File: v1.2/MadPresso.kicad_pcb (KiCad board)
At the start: 2 copper layers, 108 x 57.5 mm, 75 parts, among them J1 Conn_01x07, J2 Conn_01x03, J3 Conn_01x02, J4 Conn_01x04, Q1 BC847, Q2 BSS84, Q3 T835-600B, Q4 2N7002, Q5 T835-600B, Q6 2N7002, Q7 T835-600B, Q8 2N7002, U1 LTV-356T, U2 ADC101C021CIMK, U3 WeMos_D1_mini, U4 MID400, U5 MID400, U6 TLP160G, U7 TLP160G, U8 TLP160G

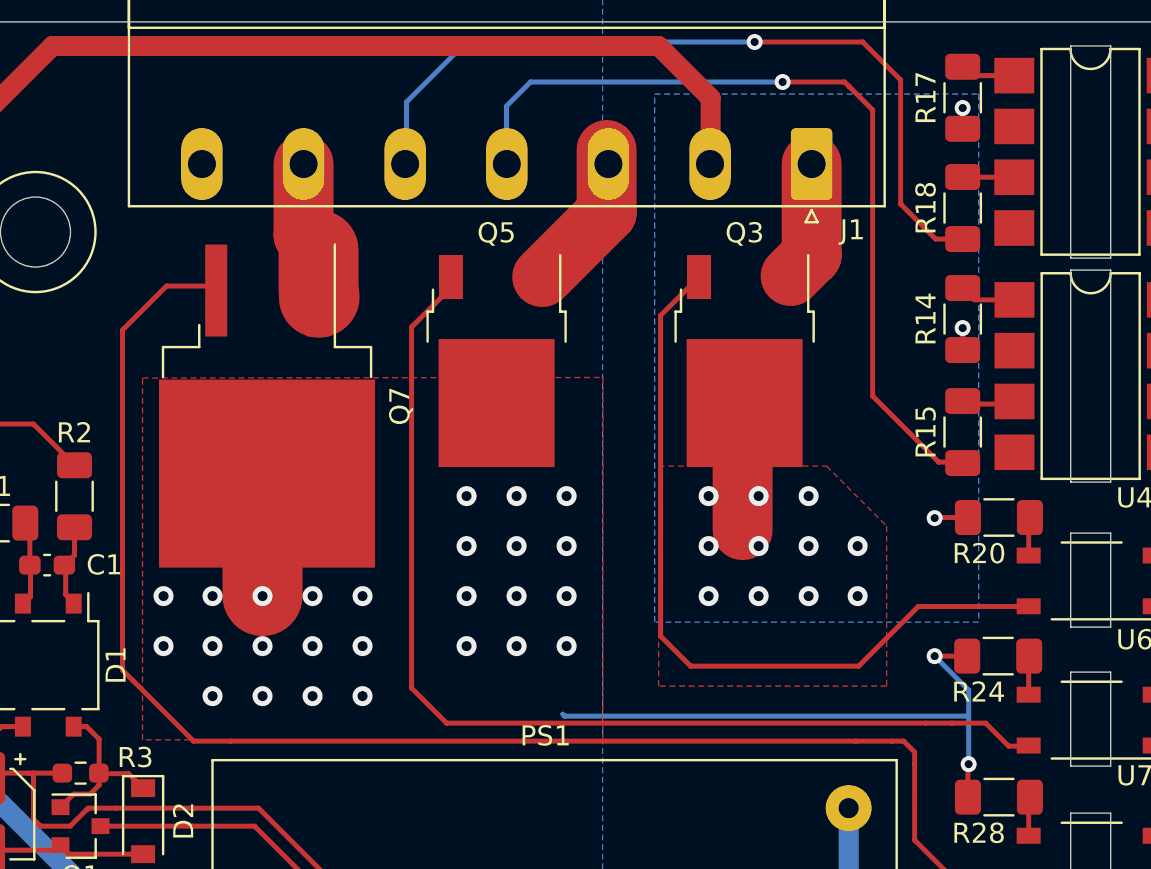
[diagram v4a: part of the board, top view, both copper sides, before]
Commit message: Revert Q7 back to DPAK
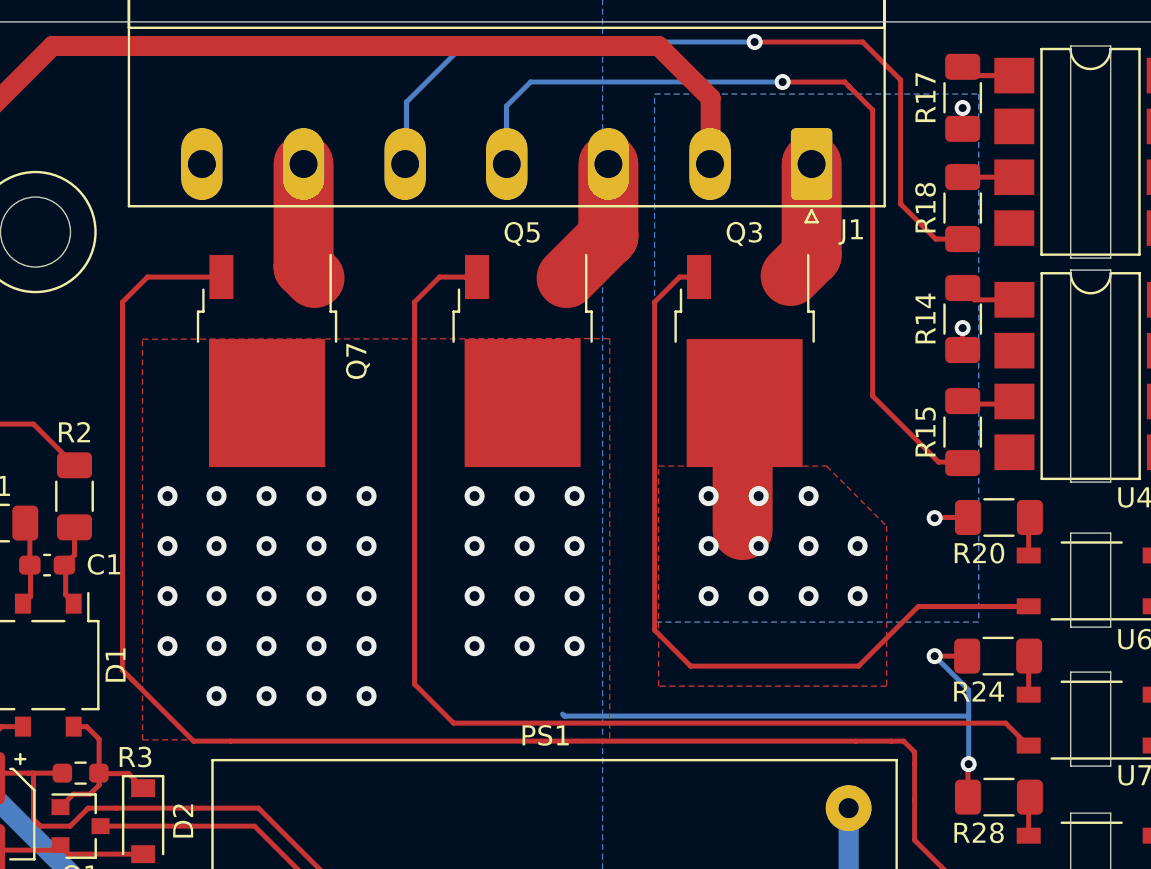
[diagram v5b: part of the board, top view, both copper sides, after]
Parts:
- Q7: footprint Package_TO_SOT_SMD:TO-263-2 -> Package_TO_SOT_SMD:TO-252-2
- moved Q7 2.25 mm to (26.8, 16.9)
- moved Q5 1.30 mm to (39.6, 16.9)
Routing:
- net LINE: track 35.7 -> 29.8 mm, vias 28 -> 38
- net Net-(Q7-Pad3): track 74.9 -> 76.2 mm
- net /VALVE: track 7.68 -> 6.57 mm
- net Net-(Q5-Pad3): track 53.4 -> 54.4 mm
- net Net-(Q3-Pad3): track 39.0 -> 39.8 mm
- net /HEATER: track 6.65 -> 5.93 mm

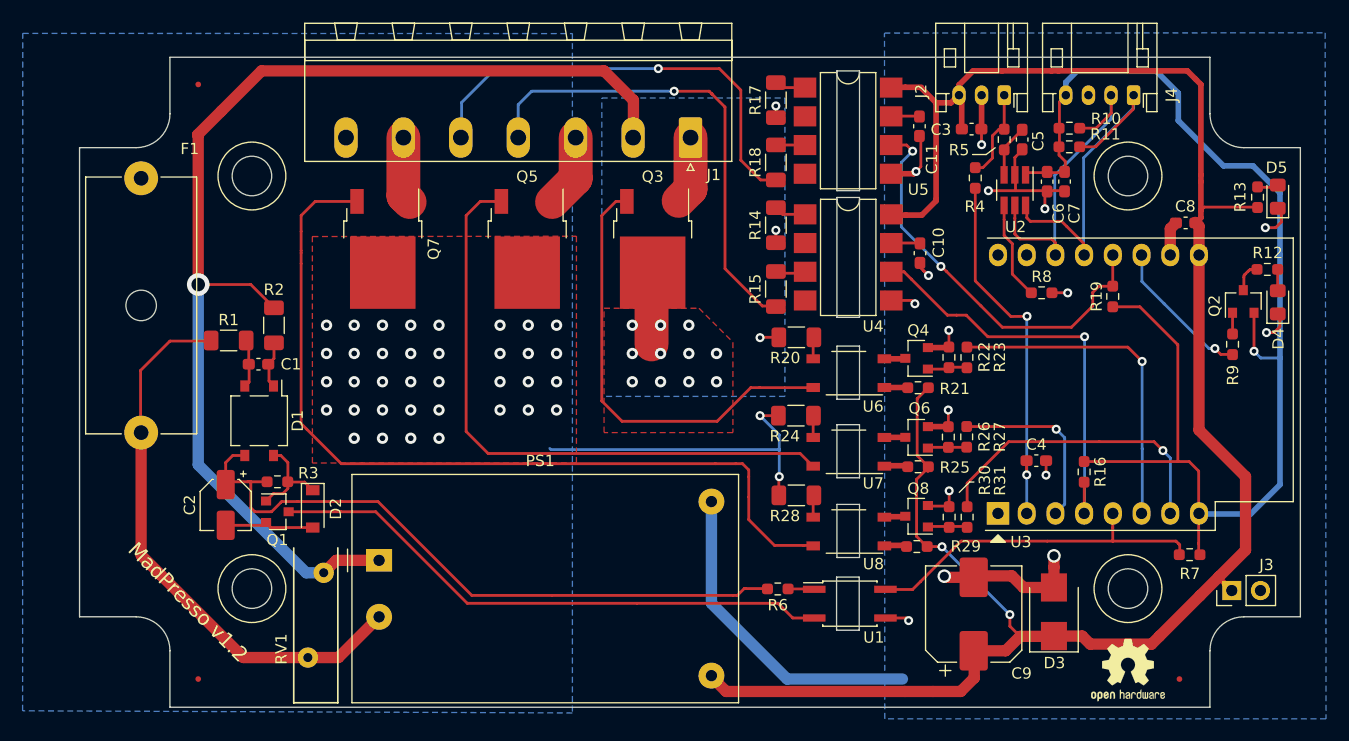
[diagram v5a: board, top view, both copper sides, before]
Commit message: trace widths and clearance details
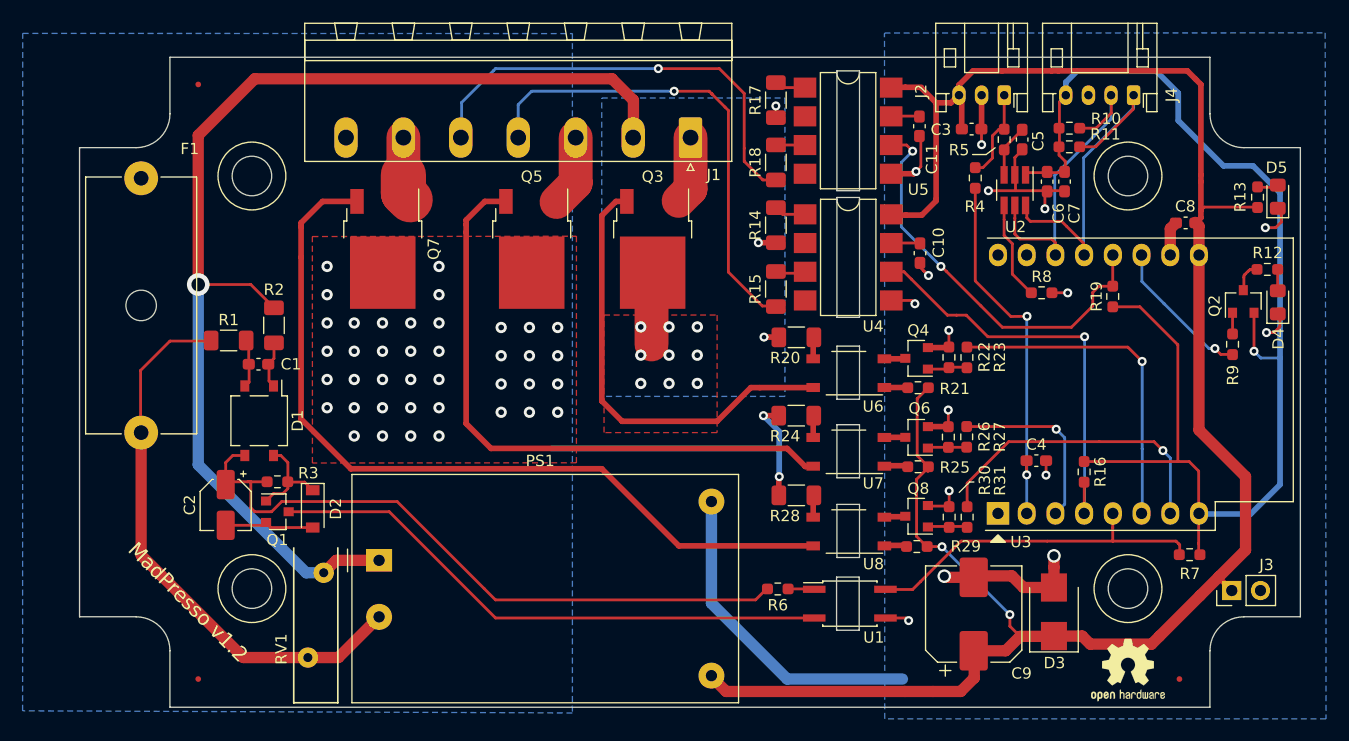
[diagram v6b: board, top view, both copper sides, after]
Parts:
- moved Q5 0.40 mm to (40.0, 16.9)
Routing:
- net Net-(Q7-Pad3): track 76.2 -> 73.0 mm
- net /HEATER: track 5.93 -> 7.60 mm
- net NEUT: track 113.1 -> 112.5 mm, vias 15 -> 13
- net LINE: track 29.8 -> 29.3 mm, vias 38 -> 42

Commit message: adc cleanups
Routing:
- net GND: track 92.2 -> 89.0 mm
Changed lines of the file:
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@@
     (property "Sheet name" "")
     (attr smd)
-    (fp_text reference "C5" (at 0.125 -1.41 -90) (layer "F.SilkS")
+    (fp_text reference "C5" (at -0.675 -1.41 -90) (layer "F.SilkS")
       (effects (font (size 1 1) (thickness 0.15)))
     )
@@
   (segment (start 86.2 46.9) (end 83.5 46.9) (width 1) (layer "F.Cu") (net 1))
   (segment (start 106.31 13.375) (end 106.31 14.57) (width 0.25) (layer "F.Cu") (net 1))
-  (segment (start 82.8 11.074634) (end 82.8 11.8) (width 0.25) (layer "F.Cu") (net 1))
   (segment (start 74.3 6.9625) (end 74.425002 7.087502) (width 0.25) (layer "F.Cu") (net 1))
   (segment (start 76.93 39.83) (end 77 39.9) (width 0.25) (layer "F.Cu") (net 1))
   (segment (start 86.0225 20.83) (end 87.41 20.83) (width 0.25) (layer "F.Cu") (net 1))
   (segment (start 106.31 14.57) (end 105.81 15.07) (width 0.25) (layer "F.Cu") (net 1))
+  (segment (start 82.74 11.29) (end 83.15 11.7) (width 0.25) (layer "F.Cu") (net 1))
+  (segment (start 85.605 11.855) (end 85.6 11.85) (width 0.25) (layer "F.Cu") (net 1))
   (segment (start 96.49 17.49) (end 96.49 15.16) (width 1) (layer "F.Cu") (net 1))
-  (segment (start 82.74 10.4) (end 82.74 8.86) (width 0.25) (layer "F.Cu") (net 1))
   (segment (start 105.81 15.07) (end 104.9 15.07) (width 0.25) (layer "F.Cu") (net 1))
   (segment (start 106.19 22.7) (end 106.19 23.83) (width 0.25) (layer "F.Cu") (net 1))
@@
   (segment (start 86.2 46.9) (end 86.2 45.1) (width 1) (layer "F.Cu") (net 1))
   (segment (start 74.425002 7.087502) (end 74.425002 9.674998) (width 0.25) (layer "F.Cu") (net 1))
-  (segment (start 85.4 13.4) (end 85.4 12) (width 0.25) (layer "F.Cu") (net 1))
-  (segment (start 82.74 8.86) (end 83.4 8.2) (width 0.25) (layer "F.Cu") (net 1))
-  (segment (start 82.8 11.8) (end 87.2 11.8) (width 0.25) (layer "F.Cu") (net 1))
+  (segment (start 83.15 11.7) (end 85.35 11.7) (width 0.25) (layer "F.Cu") (net 1))
   (segment (start 76.895 25.68) (end 76.91 25.665) (width 0.5) (layer "F.Cu") (net 1))
+  (segment (start 85.35 11.7) (end 85.6 11.95) (width 0.25) (layer "F.Cu") (net 1))
   (segment (start 82.74 10.4) (end 82.8 10.46) (width 0.25) (layer "F.Cu") (net 1))
   (segment (start 74.69 18.91) (end 74.71 18.91) (width 0.25) (layer "F.Cu") (net 1))
+  (segment (start 83.39 8.1375) (end 84.5375 8.1375) (width 0.25) (layer "F.Cu") (net 1))
   (segment (start 79.79 7.72) (end 79.8 7.73) (width 0.25) (layer "F.Cu") (net 1))
   (segment (start 71.295 49.6) (end 73.115 49.6) (width 0.25) (layer "F.Cu") (net 1))
@@
   (segment (start 89.25 3.35) (end 88.8 3.8) (width 0.25) (layer "F.Cu") (net 1))
   (segment (start 71.81 21.51) (end 73.61 21.51) (width 0.25) (layer "F.Cu") (net 1))
-  (segment (start 80.4 11.8) (end 82.8 11.8) (width 0.25) (layer "F.Cu") (net 1))
+  (segment (start 87.1375 11.855) (end 85.605 11.855) (width 0.25) (layer "F.Cu") (net 1))
   (segment (start 76.815 32.67) (end 76.86 32.715) (width 0.5) (layer "F.Cu") (net 1))
   (segment (start 87.41 20.83) (end 87.42 20.84) (width 0.25) (layer "F.Cu") (net 1))
   (segment (start 86.2 44.1) (end 86.2 45.1) (width 1) (layer "F.Cu") (net 1))
   (segment (start 87.45 11.67) (end 87.42 11.7) (width 0.25) (layer "F.Cu") (net 1))
+  (segment (start 82.74 10.4) (end 82.74 11.29) (width 0.25) (layer "F.Cu") (net 1))
   (segment (start 73.61 21.51) (end 73.9 21.8) (width 0.25) (layer "F.Cu") (net 1))
   (segment (start 75.05 25.68) (end 76.895 25.68) (width 0.5) (layer "F.Cu") (net 1))
   (segment (start 76.75 39.65) (end 76.93 39.47) (width 0.5) (layer "F.Cu") (net 1))
   (segment (start 105.67 24.35) (end 105 24.35) (width 0.25) (layer "F.Cu") (net 1))
+  (segment (start 85.6 11.8625) (end 85.6 12.85) (width 0.25) (layer "F.Cu") (net 1))
   (segment (start 74.35 18.2) (end 74.35 18.57) (width 0.25) (layer "F.Cu") (net 1))
   (segment (start 74.425002 9.674998) (end 74 10.1) (width 0.25) (layer "F.Cu") (net 1))
@@
   (segment (start 82.475 45.875) (end 79.025 45.875) (width 1) (layer "F.Cu") (net 1))
   (segment (start 79.1 46) (end 76.6 46) (width 1) (layer "F.Cu") (net 1))
+  (segment (start 85.6 12.85) (end 85.1 13.35) (width 0.25) (layer "F.Cu") (net 1))
   (segment (start 76.86 31.16) (end 76.85 31.15) (width 0.5) (layer "F.Cu") (net 1))
   (segment (start 73.115 49.6) (end 73.345 49.83) (width 0.25) (layer "F.Cu") (net 1))
@@
   (segment (start 83.5 46.9) (end 82.475 45.875) (width 1) (layer "F.Cu") (net 1))
   (segment (start 76.93 38.35) (end 76.93 39.83) (width 0.25) (layer "F.Cu") (net 1))
+  (segment (start 84.5375 8.1375) (end 84.8 8.4) (width 0.25) (layer "F.Cu") (net 1))
   (segment (start 76.6 46) (end 76.5 45.9) (width 1) (layer "F.Cu") (net 1))
-  (segment (start 82.8 10.46) (end 82.8 11.074634) (width 0.25) (layer "F.Cu") (net 1))
+  (via (at 84.8 8.4) (size 0.8) (drill 0.4) (layers "F.Cu" "B.Cu") (net 1))
   (via (at 85.5 36.96) (size 0.8) (drill 0.4) (layers "F.Cu" "B.Cu") (remove_unused_layers) (keep_end_layers) (net 1))
   (via (at 75.1 19.3) (size 0.8) (drill 0.4) (layers "F.Cu" "B.Cu") (remove_unused_layers) (keep_end_layers) (net 1))
@@
   (via (at 86.2 44.1) (size 1.2) (drill 0.8) (layers "F.Cu" "B.Cu") (remove_unused_layers) (keep_end_layers) (net 1))
   (via (at 105 24.35) (size 0.8) (drill 0.4) (layers "F.Cu" "B.Cu") (remove_unused_layers) (keep_end_layers) (net 1))
-  (via (at 85.4 13.4) (size 0.8) (drill 0.4) (layers "F.Cu" "B.Cu") (remove_unused_layers) (keep_end_layers) (net 1))
+  (via (at 85.1 13.35) (size 0.8) (drill 0.4) (layers "F.Cu" "B.Cu") (remove_unused_layers) (keep_end_layers) (net 1))
   (via (at 76.85 31.2) (size 0.8) (drill 0.4) (layers "F.Cu" "B.Cu") (remove_unused_layers) (keep_end_layers) (net 1))
   (via (at 74 10.1) (size 0.8) (drill 0.4) (layers "F.Cu" "B.Cu") (remove_unused_layers) (keep_end_layers) (net 1))
@@
   (via (at 87.42 20.84) (size 0.8) (drill 0.4) (layers "F.Cu" "B.Cu") (remove_unused_layers) (keep_end_layers) (net 1))
   (via (at 73.345 49.83) (size 0.8) (drill 0.4) (layers "F.Cu" "B.Cu") (remove_unused_layers) (keep_end_layers) (net 1))
-  (via (at 80.4 11.8) (size 0.8) (drill 0.4) (layers "F.Cu" "B.Cu") (remove_unused_layers) (keep_end_layers) (net 1))
   (via (at 104.9 15.07) (size 0.8) (drill 0.4) (layers "F.Cu" "B.Cu") (remove_unused_layers) (keep_end_layers) (net 1))
   (via (at 79.8 7.73) (size 0.8) (drill 0.4) (layers "F.Cu" "B.Cu") (remove_unused_layers) (keep_end_layers) (net 1))
